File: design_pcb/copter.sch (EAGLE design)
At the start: 54 parts, among them U1 ATMEGA328P-AU, U2 ITG-3200, U3 ADXL345, U4 3.3V, U5 HC_05, U6 IRF9362PBF, U7 IRF9362PBF, U8 HMC5883LSMD, U9 INA169, Y1 8MHZ

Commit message: Add test programs
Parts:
- removed C1: (no value), rcl:C-EUC0402
- removed C1_3V3, C1_U4: 4.7uF, SparkFun:CAP0402-CAP
- removed C2: 0.1uF, SparkFun-Passives:CAP0603-CAP
- removed C2_3V3: 0.1uF, SparkFun:CAP0402-CAP
- removed GND_PAD, VIN_PAD: (no value), wirepad:1,6/0,8
- removed R1: (no value), rcl:R-EU_R0402
- removed R2: 10k, SparkFun-Resistors:RESISTOR0603
- removed R3: (no value), SparkFun-Resistors:RESISTORPTH-2W
- removed R4: (no value), SparkFun-Resistors:RESISTORPTH-1/4W
- removed R5: 10, SparkFun-Resistors:RESISTOR1206
- removed U4: 3.3V, SparkFun:V_REG_LDOSMD
- added C1_3V1, C1_U9: 4.7uF, SparkFun:CAP0402-CAP
- added C1_U10: 0.1uF, SparkFun-Passives:CAP0603-CAP
- added C2_3V1: 0.1uF, SparkFun:CAP0402-CAP
- added LED1, LED2, LED3, LED4: (no value), led:LED3MM
- added RLOAD: 10k, SparkFun-Resistors:RESISTOR0603
- added RSHUNT_1, RSHUNT_2: (no value), resistor:R-EU_0309/10
- added RST_C: (no value), rcl:C-EUC0402
- added RST_R: (no value), rcl:R-EU_R0402
- added U10: INA169, SparkFun-AnalogIC:INA169
- added VBAT+, VBAT-: (no value), wirepad:1,6/0,8
- U9: value INA169 -> 3.3V; device SparkFun-AnalogIC:INA169 -> SparkFun:V_REG_LDOSMD
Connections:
- net N$15 renamed MTR4
- net N$31 renamed MTR3
- removed net VOUT: R2.2, R4.2, U9.OUT
- new net I_MEASURE: RLOAD.2, U1.PC1, U10.OUT
- new net LED1: LED3.A, U1.PB0
- new net LED2: LED4.A, U1.PB4
- new net LED3: LED1.A, U1.PD7
- new net LED4: LED2.A, U1.PD4
- net +3V3: now also C1_3V1.1, C2_3V1.1, U9.OUT; no longer C1_3V3.1, C2.2, C2_3V3.1, R3.1, R5.1, U4.OUT, U9.V+, U9.VIN+
- net +5V: now also C1_U10.2, RSHUNT_1.1, RSHUNT_2.1, U10.V+, U10.VIN+, VBAT+.P; no longer C1_U1.1, C1_U4.1, C2_U1.1, MTR1_2.P, MTR3_2.P, PWR.A, R1.2, RN1A.1, RN1B.1, U1.AVCC, U1.VCC, U1.VCC_2, U4.EN, U4.IN, U6.S2, U7.S2, VIN_PAD.P
- net DTR: now also RST_C.2; no longer C1.2
- net GND: now also C1_3V1.2, C1_U10.1, C1_U9.2, C2_3V1.2, LED1.C, LED2.C, LED3.C, LED4.C, RLOAD.1, U10.GND, VBAT-.P; no longer C1_3V3.2, C1_U4.2, C2.1, C2_3V3.2, GND_PAD.P, R2.1, R4.1, U4.GND
- net RST: now also RST_C.1, RST_R.1; no longer C1.1, R1.1
- net VCC: now also C1_U1.1, C1_U9.1, C2_U1.1, MTR1_2.P, MTR3_2.P, PWR.A, RN1A.1, RN1B.1, RSHUNT_1.2, RSHUNT_2.2, RST_R.2, U1.AVCC, U1.VCC, U1.VCC_2, U10.VIN-, U6.S2, U7.S2, U9.EN, U9.IN; no longer R3.2, R5.2, U9.VIN-
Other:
- note added: "3v3 SUPPLY"
- note added: "CURRENT MEASURE"
- note added: "EXTERNAL SUPPLY"
- note added: "JTAG"
- note added: "VOLTAGE MEASURE"
- note removed: "IS"
- note removed: "RS"
- moved on the sheet: C1_5V1, C1_U1, C1_U2, C1_U3, C1_U8, C2_5V1, C2_U1, C2_U3, C3_U8, C4_U8, C6_U2, C7_U2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

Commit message: Update schematic and PCB
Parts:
- removed C1_U10: 0.1uF, SparkFun-Passives:CAP0603-CAP
- removed C1_U9: 4.7uF, SparkFun:CAP0402-CAP
- removed J1: (no value), SparkFun-Connectors:M05PTH
- removed LED1, LED2, LED3, LED4: (no value), led:LED3MM
- removed R6: 5.1K, resistor:R-EU_R0402
- removed R7: 1.2K, resistor:R-EU_R0402
- removed RLOAD: 10k, SparkFun-Resistors:RESISTOR0603
- removed RSHUNT_1, RSHUNT_2: (no value), resistor:R-EU_0309/10
- removed RST_C: (no value), rcl:C-EUC0402
- removed RST_R: (no value), rcl:R-EU_R0402
- removed VBAT+, VBAT-: (no value), wirepad:1,6/0,8
- added C1: (no value), rcl:C-EUC0402
- added C1_U5: 4.7uF, SparkFun:CAP0402-CAP
- added C_IMEASURE: 0.1uF, SparkFun-Passives:CAP0603-CAP
- added GND_PAD, VIN_PAD: (no value), wirepad:1,6/0,8
- added R1: (no value), rcl:R-EU_R0402
- added R1_DIV: 5.1K, resistor:R-EU_R0402
- added R2_DIV: 1.2K, resistor:R-EU_R0402
- added R_LOAD: (no value), resistor:R-EU_0309/10
- added R_SHUNT: 10k, SparkFun-Resistors:RESISTOR0603
- added X1: 05-JST-B5B-XH-A, bt_con-jst-xh:05-JST-B5B-XH-A
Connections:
- net MTR3 renamed N$31
- net MTR4 renamed N$15
- removed net LED1: LED3.A, U1.PB0
- removed net LED2: LED4.A, U1.PB4
- removed net LED3: LED1.A, U1.PD7
- removed net LED4: LED2.A, U1.PD4
- net +3V3: now also C_IMEASURE.2, U10.V+
- net +5V: now also C1_U1.1, C1_U5.1, C2_U1.1, PWR.A, R1.2, R1_DIV.2, RN1A.1, RN1B.1, R_LOAD.1, U1.AVCC, U1.VCC, U1.VCC_2, U9.EN, U9.IN, VIN_PAD.P, X1-5.1; no longer C1_U10.2, J1.5, R6.2, RSHUNT_1.1, RSHUNT_2.1, U10.V+, VBAT+.P
- net D0/RX: now also X1-2.1; no longer J1.2
- net D1/TX: now also X1-3.1; no longer J1.3
- net DTR: now also C1.2, X1-4.1; no longer J1.4, RST_C.2
- net GND: now also C1_U5.2, C_IMEASURE.1, GND_PAD.P, R2_DIV.1, R_SHUNT.1, X1-1.1; no longer C1_U10.1, C1_U9.2, J1.1, LED1.C, LED2.C, LED3.C, LED4.C, R7.1, RLOAD.1, VBAT-.P
- net I_MEASURE: now also R_SHUNT.2; no longer RLOAD.2
- net RST: now also C1.1, R1.1; no longer RST_C.1, RST_R.1
- net VCC: now also R_LOAD.2; no longer C1_U1.1, C1_U9.1, C2_U1.1, PWR.A, RN1A.1, RN1B.1, RSHUNT_1.2, RSHUNT_2.2, RST_R.2, U1.AVCC, U1.VCC, U1.VCC_2, U9.EN, U9.IN
- net V_MEASURE: now also R1_DIV.1, R2_DIV.2; no longer R6.1, R7.2
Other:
- note added: "3v3 REGULATOR"
- note added: "CPU"
- note added: "POWER"
- note added: "SPI"
- note removed: "3v3 SUPPLY"
- note removed: "EXTERNAL SUPPLY"
- note removed: "JTAG"
- moved on the sheet: C1_3V1, C1_5V1, C1_U1, C2_3V1, C2_5V1, C2_U1, C_REF, MTR1_1, MTR1_2, MTR2_1, MTR2_2, MTR3_1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

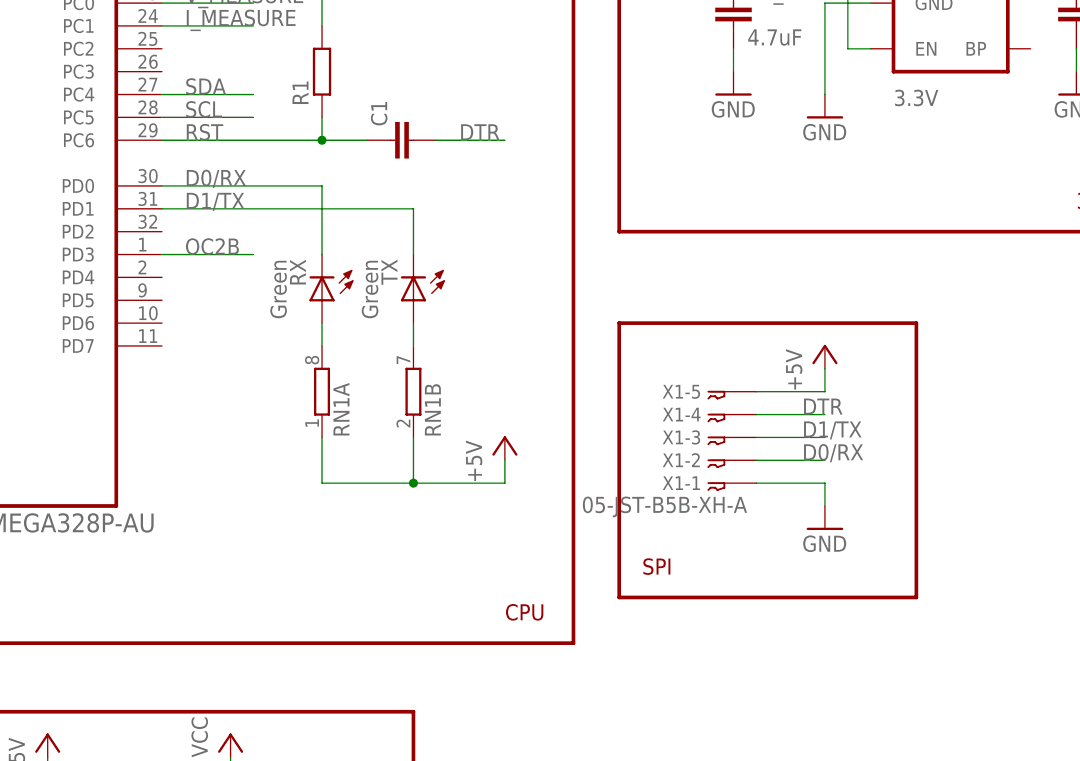
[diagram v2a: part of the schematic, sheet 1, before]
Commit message: move some components
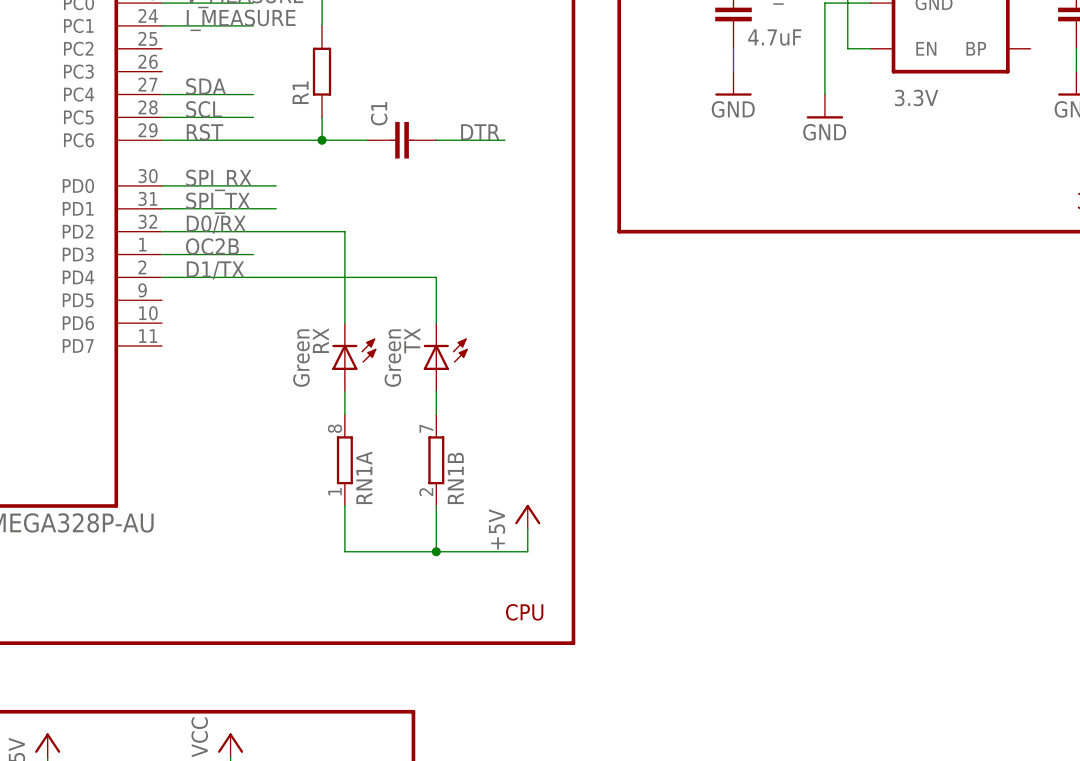
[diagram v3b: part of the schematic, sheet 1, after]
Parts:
- removed X1: 05-JST-B5B-XH-A, bt_con-jst-xh:05-JST-B5B-XH-A
- added J1: USB-MINIB-5PIN, SparkFun-Connectors:USB-MINIB-5PIN
- added R2, R3: 1k, resistor:R-EU_R0402
- added U$1: CH340G, usb-serial:CH340G
- added U$2: CSTCV, murata-cstcc-cstce-cstcr-cstcv-resonators:CSTCV
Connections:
- new net D+: J1.D+, U$1.D+
- new net D-: J1.D-, U$1.D-
- new net N$1: R2.2, U$1.TX
- new net N$16: U$1.XI, U$2.IN
- new net N$4: R3.2, U$1.RX
- new net N$9: U$1.XO, U$2.OUT
- new net SPI_RX: R3.1, U1.PD0
- new net SPI_TX: R2.1, U1.PD1
- net +5V: now also J1.VBUS, U$1.VCC; no longer X1-5.1
- net D0/RX: now also U1.PD2; no longer U1.PD0, X1-2.1
- net D1/TX: now also U1.PD4; no longer U1.PD1, X1-3.1
- net DTR: now also U$1.DTR; no longer X1-4.1
- net GND: now also J1.GND, U$1.GND, U$2.GND; no longer X1-1.1
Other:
- note removed: "SPI"
- moved on the sheet: RN1A, RN1B, RX, TX

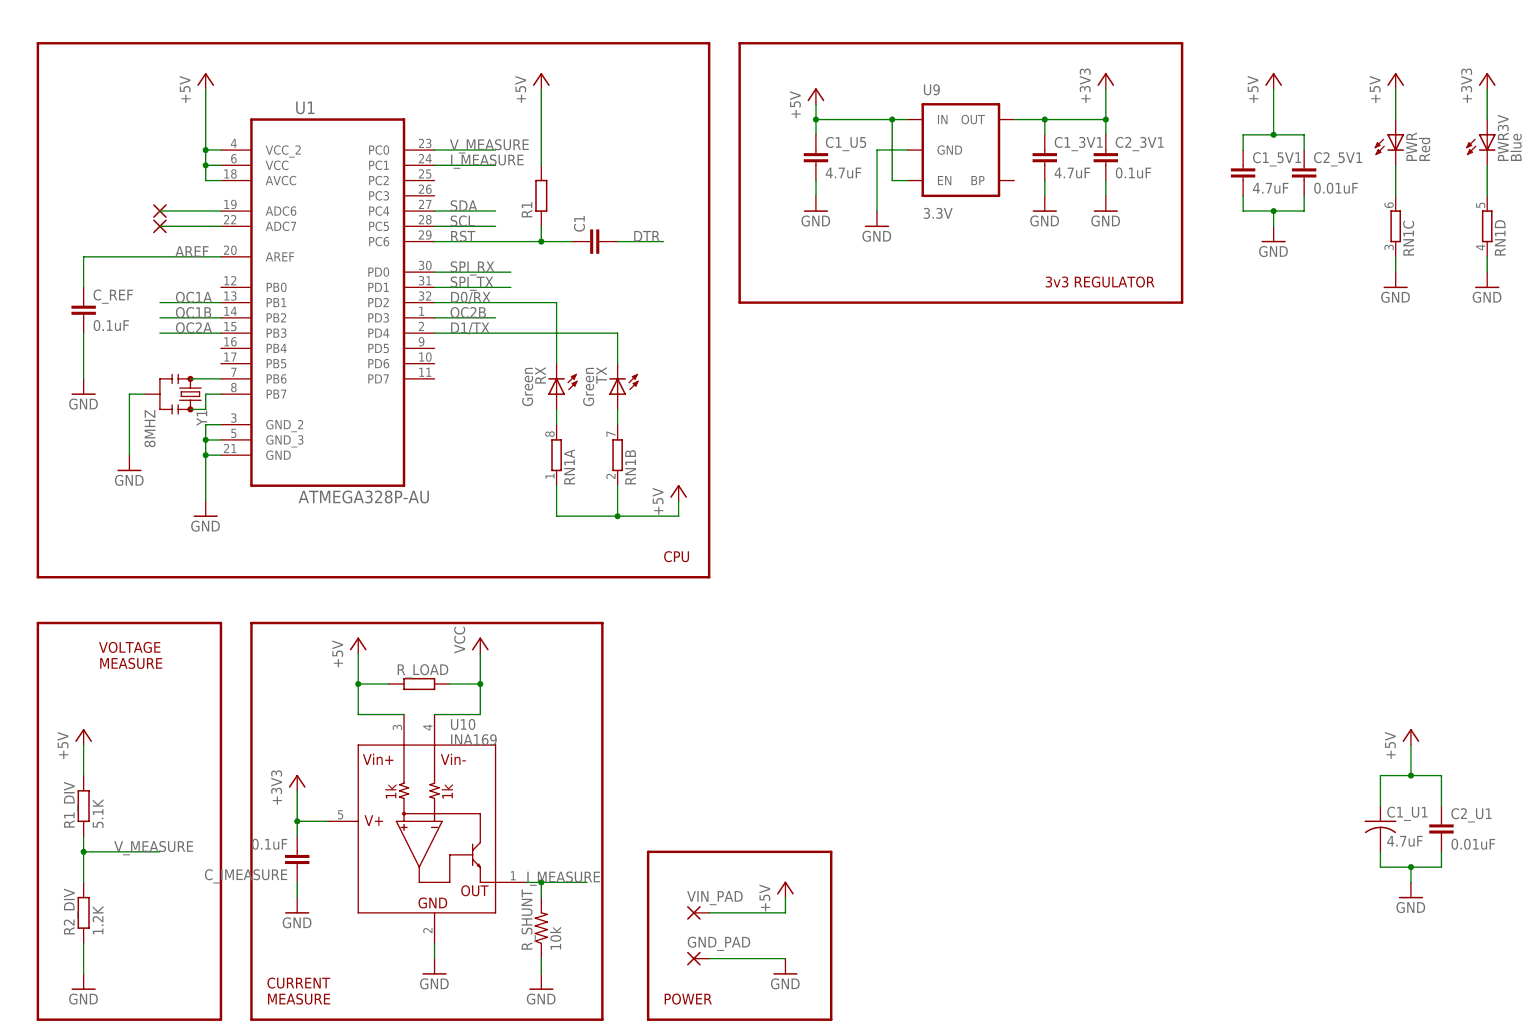
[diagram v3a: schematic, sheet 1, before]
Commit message: replace *4 resistor with 4 separate resistors
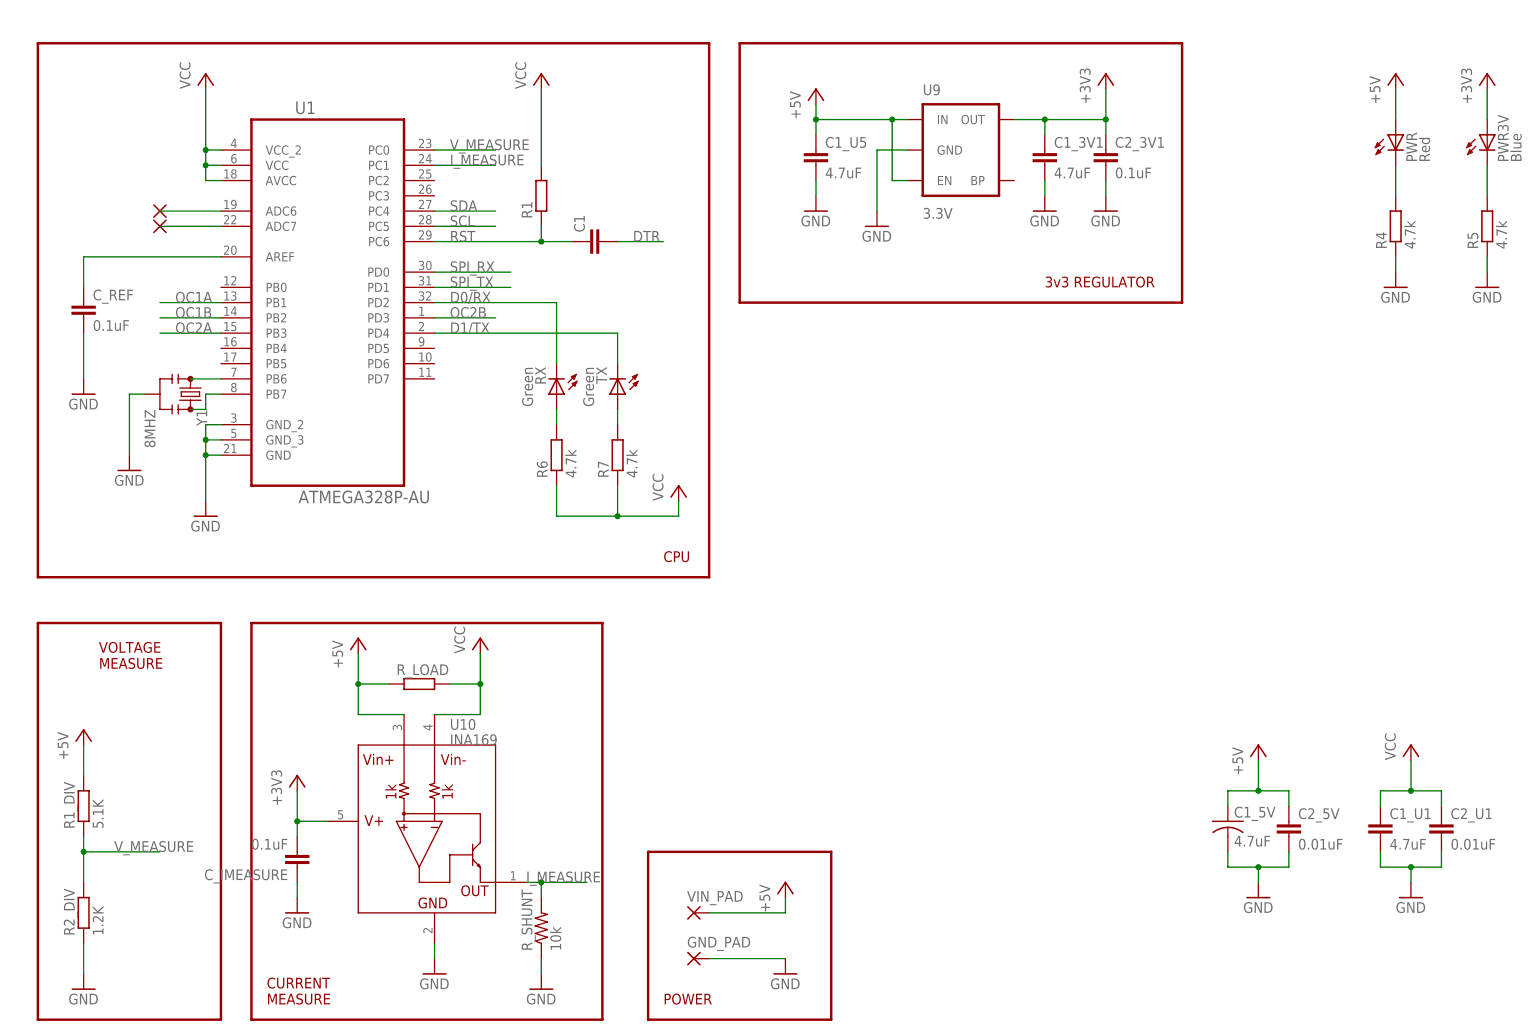
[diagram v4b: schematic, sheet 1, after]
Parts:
- removed C1_5V1: 4.7uF, resistor:C-EUC1206
- removed C2_5V1: 0.01uF, resistor:C-EUC0402
- removed RN1: (no value), resistor-dil:4R-NEXB38V
- added C1_5V: 4.7uF, rcl:C-USC1210K
- added C2_5V: 0.01uF, resistor:C-EUC0402
- added R4, R5, R6, R7: 4.7k, rcl:R-EU_R0402
- C1_U1: device rcl:C-USC1210K -> resistor:C-EUC1206
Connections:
- net AREF renamed N$17
- net +5V: now also C1_5V.1, C2_5V.1; no longer C1_5V1.1, C1_U1.1, C2_5V1.1, C2_U1.1, R1.2, RN1A.1, RN1B.1, U$1.VCC, U1.AVCC, U1.VCC, U1.VCC_2
- net GND: now also C1_5V.2, C2_5V.2, R4.1, R5.1; no longer C1_5V1.2, C2_5V1.2, RN1C.1, RN1D.1
- net N$3: now also R7.2; no longer RN1B.2
- net N$5: now also R6.2; no longer RN1A.2
- net N$6: now also R4.2; no longer RN1C.2
- net N$8: now also R5.2; no longer RN1D.2
- net VCC: now also C1_U1.1, C2_U1.1, R1.2, R6.1, R7.1, U$1.VCC, U1.AVCC, U1.VCC, U1.VCC_2

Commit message: add breakout boards
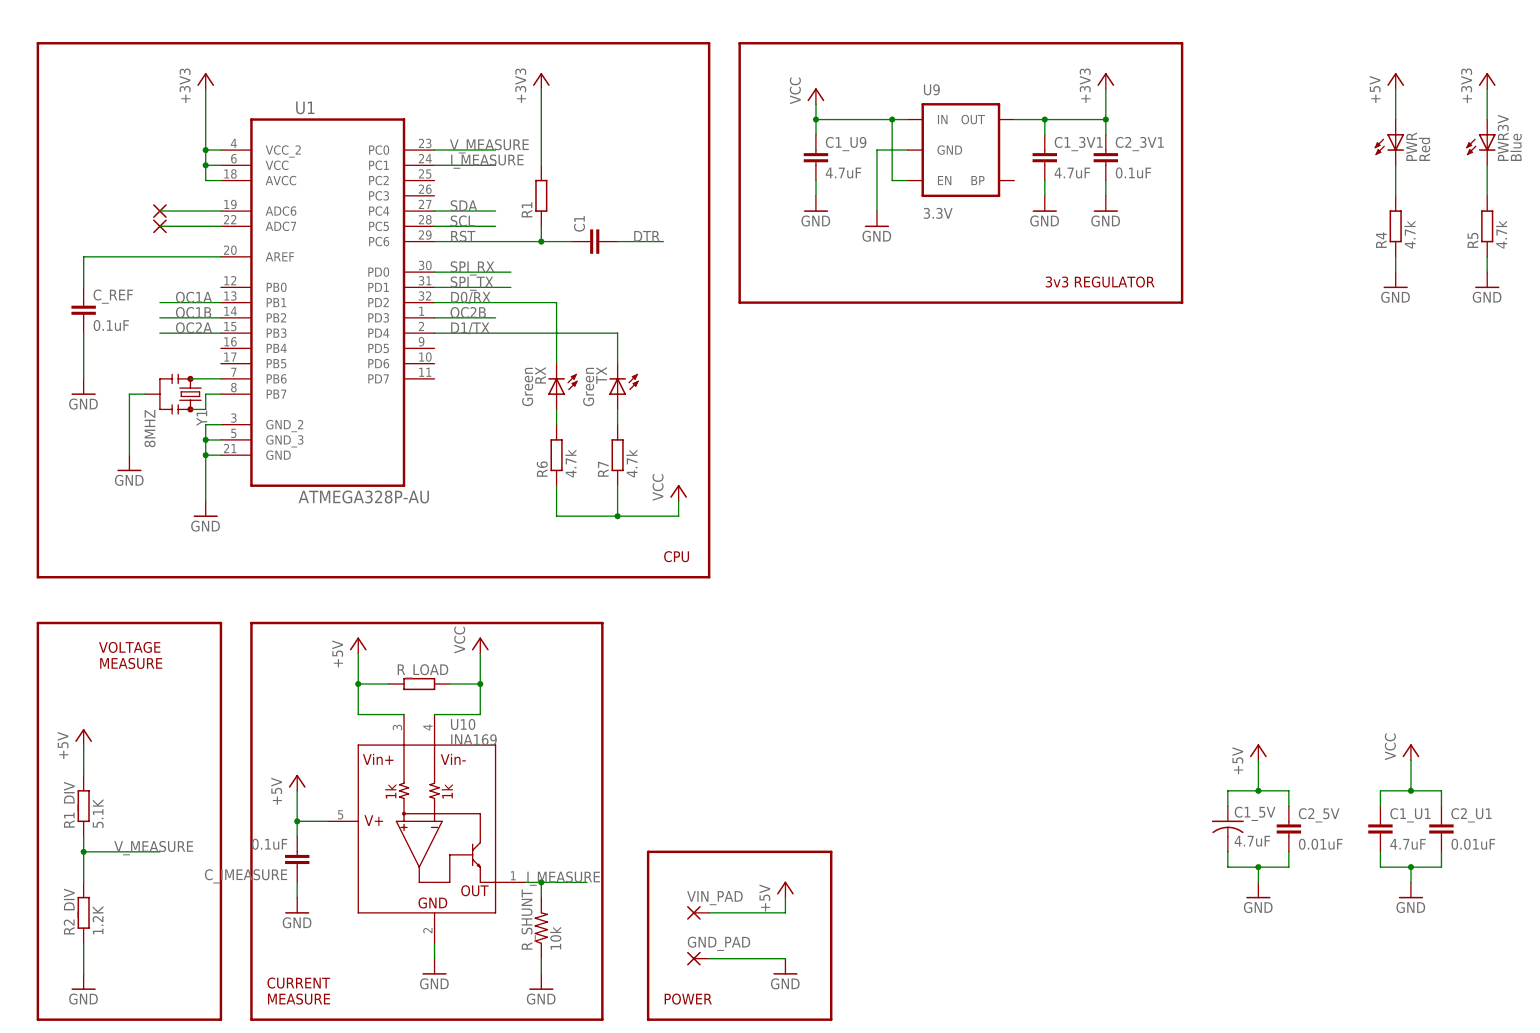
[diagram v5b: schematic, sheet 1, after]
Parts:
- renumbered C1_U5 to C1_U9
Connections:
- net +3V3: now also R1.2, U1.AVCC, U1.VCC, U1.VCC_2; no longer C_IMEASURE.2, U10.V+
- net +5V: now also C_IMEASURE.2, U10.V+; no longer C1_U9.1, U9.EN, U9.IN
- net VCC: now also C1_U9.1, U9.EN, U9.IN; no longer R1.2, U1.AVCC, U1.VCC, U1.VCC_2
